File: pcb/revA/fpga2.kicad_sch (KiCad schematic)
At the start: 22 parts, among them J1 FPGA JTAG, U1 XC6SLX25-FTG256, U2 W25Q128JVS, X1 50 MHz

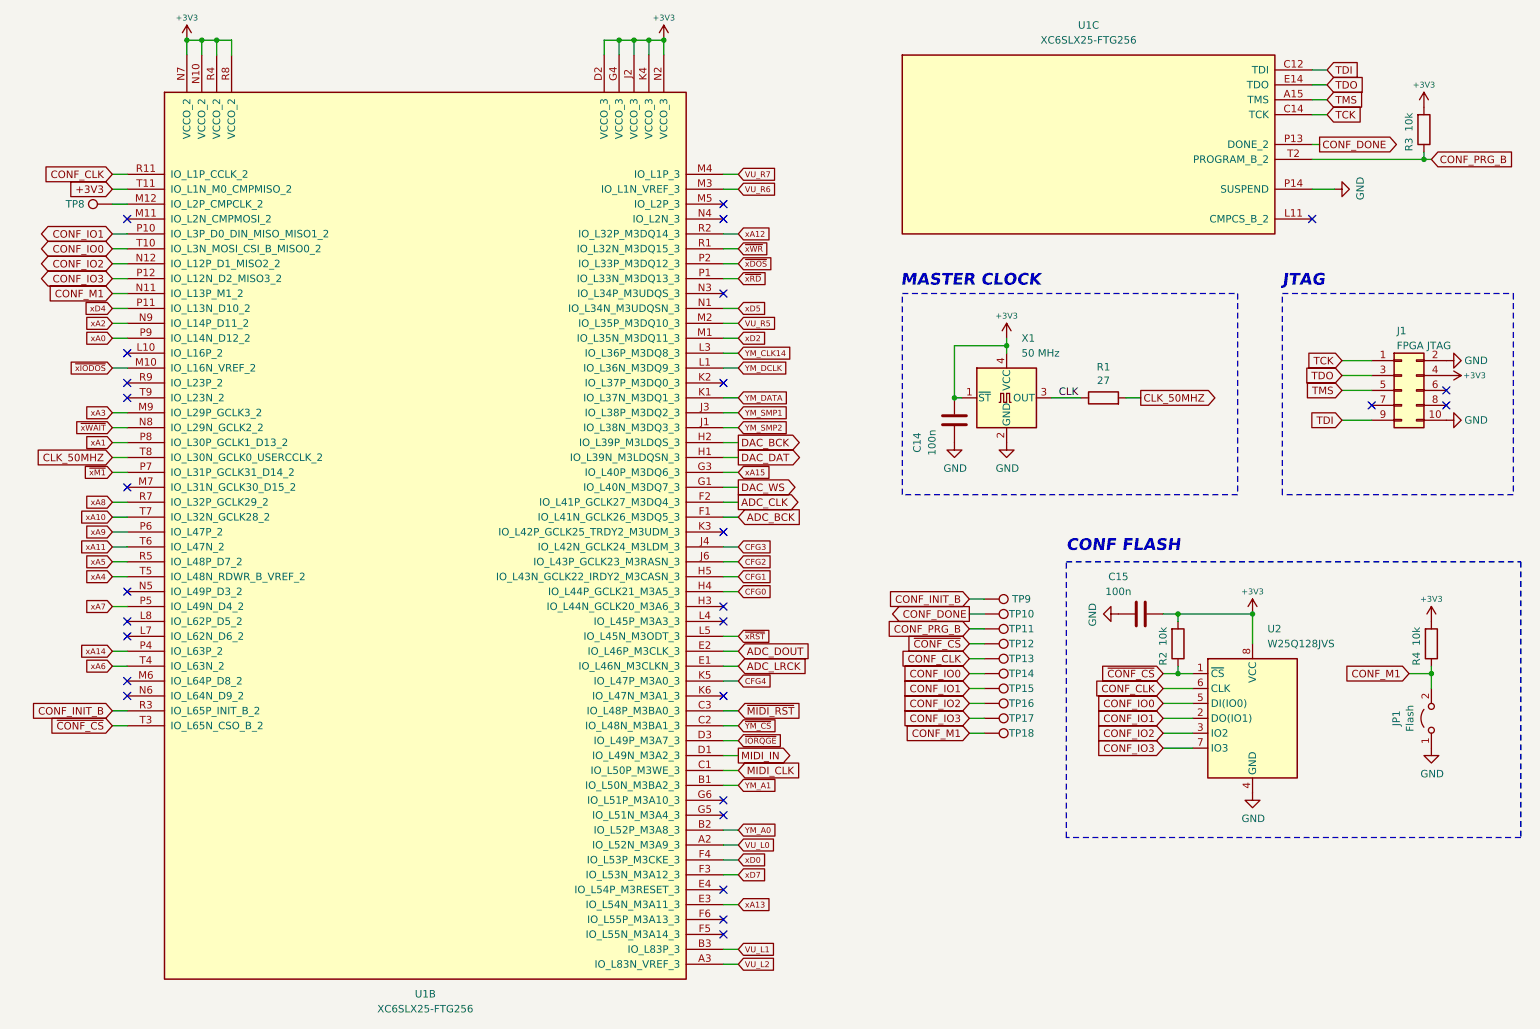
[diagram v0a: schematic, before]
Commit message: Updated gerbers to min 0.2/0.45 vias, firmware build for xc6slx16
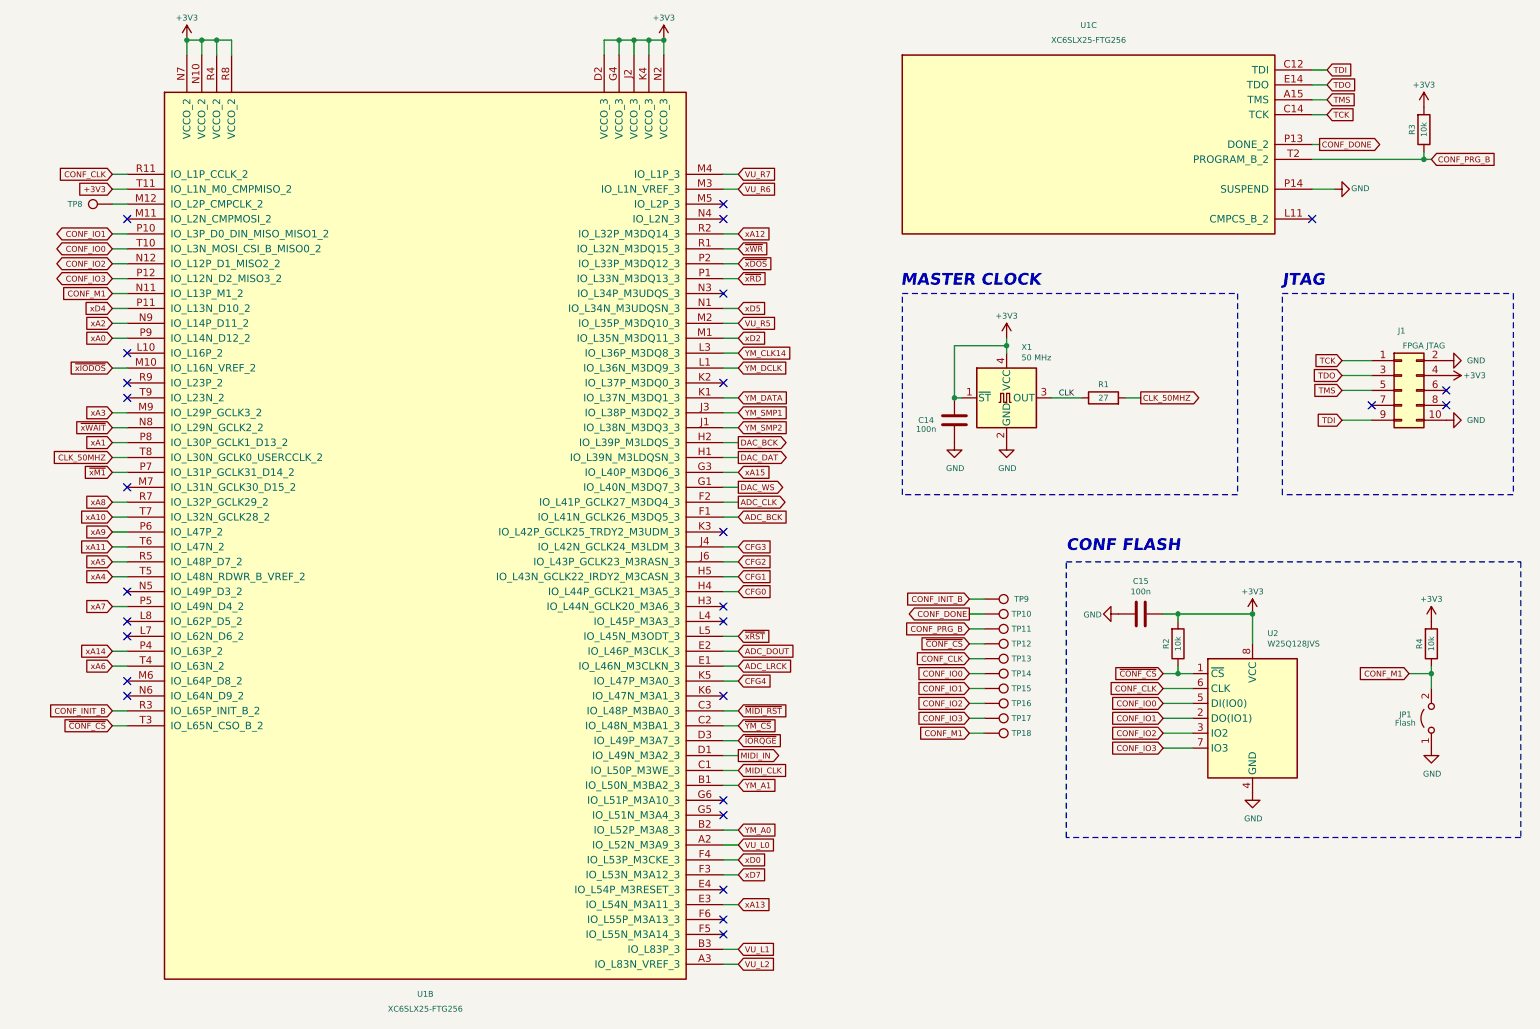
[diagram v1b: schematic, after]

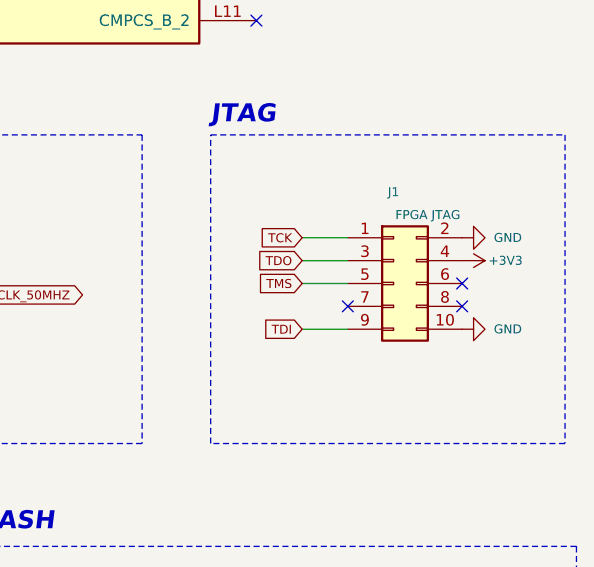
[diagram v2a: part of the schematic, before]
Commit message: Updated revA (cosmetic changes)
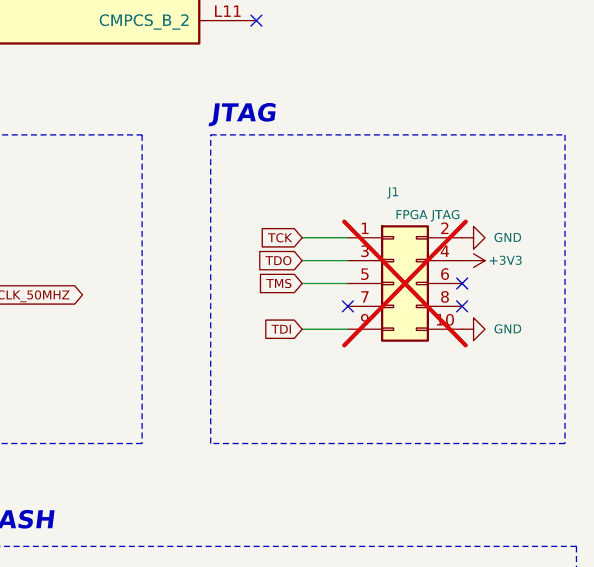
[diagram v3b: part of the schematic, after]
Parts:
- J1: now not fitted; now left out of the parts list
- JP1, TP10, TP11, TP12, TP13, TP14, TP15, TP16, TP17, TP18, TP8, TP9: now left out of the parts list
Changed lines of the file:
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@@
 		(body_style 1)
 		(exclude_from_sim no)
-		(in_bom yes)
+		(in_bom no)
 		(on_board yes)
 		(in_pos_files yes)
@@
 		(body_style 1)
 		(exclude_from_sim no)
-		(in_bom yes)
+		(in_bom no)
 		(on_board yes)
 		(in_pos_files yes)
@@
 		(body_style 1)
 		(exclude_from_sim no)
-		(in_bom yes)
+		(in_bom no)
 		(on_board yes)
 		(in_pos_files yes)
@@
 		(body_style 1)
 		(exclude_from_sim no)
-		(in_bom yes)
+		(in_bom no)
 		(on_board yes)
 		(in_pos_files yes)
@@
 		(body_style 1)
 		(exclude_from_sim no)
-		(in_bom yes)
+		(in_bom no)
 		(on_board yes)
 		(in_pos_files yes)
@@
 		(body_style 1)
 		(exclude_from_sim no)
-		(in_bom yes)
+		(in_bom no)
 		(on_board yes)
 		(in_pos_files yes)
@@
 		(body_style 1)
 		(exclude_from_sim no)
-		(in_bom yes)
+		(in_bom no)
 		(on_board yes)
 		(in_pos_files yes)
@@
 		(body_style 1)
 		(exclude_from_sim no)
-		(in_bom yes)
+		(in_bom no)
 		(on_board yes)
 		(in_pos_files yes)
@@
 		(body_style 1)
 		(exclude_from_sim no)
-		(in_bom yes)
+		(in_bom no)
 		(on_board yes)
 		(in_pos_files yes)
@@
 		(body_style 1)
 		(exclude_from_sim no)
-		(in_bom yes)
+		(in_bom no)
 		(on_board yes)
 		(in_pos_files yes)
@@
 		(body_style 1)
 		(exclude_from_sim no)
-		(in_bom yes)
+		(in_bom no)
 		(on_board yes)
 		(in_pos_files yes)
@@
 		(body_style 1)
 		(exclude_from_sim no)
-		(in_bom yes)
+		(in_bom no)
 		(on_board yes)
 		(in_pos_files yes)
@@
 		(body_style 1)
 		(exclude_from_sim no)
-		(in_bom yes)
+		(in_bom no)
 		(on_board yes)
 		(in_pos_files yes)
-		(dnp no)
+		(dnp yes)
 		(property "Reference" "J1"
 			(at 259.08 74.93 0)
